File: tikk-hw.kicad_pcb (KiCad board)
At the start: 4 copper layers, 18.1 x 39 mm, 142 parts, among them J1 51281-0598, P6 ZX-SH1.0-4PWT, SW1 TS24CA, SW2 TS24CA, U1 IS31FL3731-QFLS2-TR, U2 LIS2DH12TR, U3 Tenstar nRF52840, U4 CP6208DTR(XBLW), U5 TMP102AIDRLR, U6 CP6208DTR(XBLW)

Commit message: finished initial layout
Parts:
- added C3: CC0402KRX7R7BB104, easyeda2kicad:C0402, F.Cu at (167.6, 108.7)
- added R3: RC0402FR-0720KL, easyeda2kicad:R0402, F.Cu at (168.1, 112.9)
- added R4: RC0402FR-0720KL, easyeda2kicad:R0402, F.Cu at (158.7, 121.4)
- added R5: RC0402FR-0720KL, easyeda2kicad:R0402, F.Cu at (158.3, 116.4)
- added R6: RC0402FR-07100KL, easyeda2kicad:R0402, F.Cu at (160.5, 106.3)
- added R7: RC0402FR-070RL, easyeda2kicad:R0402, F.Cu at (160.5, 107.5)
- moved TP4 20.2 mm to (163.7, 118.0)
- moved TP1 14.8 mm to (168.5, 118.6)
- moved TP3 14.1 mm to (168.5, 116.6)
- moved C10 5.61 mm to (166.3, 104.6)
- moved C12 0.86 mm to (163.1, 114.5), turned to 90 degrees
- moved C14 0.71 mm to (165.4, 117.3)
- moved C13 0.71 mm to (162.0, 117.3)
- moved C11 0.66 mm to (160.0, 118.6), turned to 180 degrees
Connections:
- C10 pad 1: unconnected-(C10-Pad1) -> EXT_VCC
- C10 pad 2: unconnected-(C10-Pad2) -> GND
- C11 pad 1: unconnected-(C11-Pad1) -> EXT_VCC
- C11 pad 2: unconnected-(C11-Pad2) -> GND
- C12 pad 2: Net-(U1-VCC) -> EXT_VCC
- C2 pad 2: Net-(U1-VCC) -> EXT_VCC
- P6 pad 1: unconnected-(P6-Pad1) -> SCL
- P6 pad 2: unconnected-(P6-Pad2) -> SDA
- P6 pad 3: unconnected-(P6-Pad3) -> EXT_VCC
- P6 pad 4: unconnected-(P6-Pad4) -> GND
- P6 pad 5: unconnected-(P6-Pad5) -> GND
- P6 pad 6: unconnected-(P6-Pad6) -> GND
- SW1 pad 1: unconnected-(SW1-Pad1) -> GND
- SW1 pad 4: RESET -> USER
- SW2 pad 1: unconnected-(SW2-Pad1) -> GND
- U1 pad 16: unconnected-(U1-C_FILT-Pad16) -> Net-(U1-C_FILT)
- U1 pad 18: unconnected-(U1-AD-Pad18) -> GND
- U1 pad 2: Net-(U1-VCC) -> EXT_VCC
- U1 pad 29: unconnected-(U1-EP-Pad29) -> GND
- U1 pad 6: unconnected-(U1-R-EXT-Pad6) -> Net-(U1-R-EXT)
- U2 pad 1: unconnected-(U2-SCL/SPC-Pad1) -> SCL
- U2 pad 10: unconnected-(U2-VDD_IO-Pad10) -> EXT_VCC
- U2 pad 11: unconnected-(U2-INT2-Pad11) -> IMU_INT_2
- U2 pad 12: unconnected-(U2-INT1-Pad12) -> IMU_INT_1
- U2 pad 2: unconnected-(U2-CS-Pad2) -> Net-(U2-CS)
- U2 pad 3: unconnected-(U2-SDO/SA0-Pad3) -> Net-(U2-SDO/SA0)
- U2 pad 4: unconnected-(U2-SDA/SDI/SDO-Pad4) -> SDA
- U2 pad 5: unconnected-(U2-RES-Pad5) -> GND
- U2 pad 6: unconnected-(U2-GND-Pad6) -> GND
- U2 pad 7: unconnected-(U2-GND-Pad7) -> GND
- U2 pad 8: unconnected-(U2-GND-Pad8) -> GND
- U2 pad 9: unconnected-(U2-VDD-Pad9) -> EXT_VCC
- U3 pad 10: /P1.11 -> TMP102_ALERT
- U3 pad 19: /P0.22 -> IMU_INT_2
- U3 pad 20: /P0.24 -> IMU_INT_1
- U3 pad 22: /P0.13 -> USER
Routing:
- net SDA: track 0.00 -> 49.6 mm, vias 0 -> 3
- net SCL: track 0.00 -> 45.9 mm, vias 0 -> 6
- net /CB1: track 10.4 -> 36.2 mm, vias 0 -> 8
- net /CB3: track 10.4 -> 35.6 mm, vias 0 -> 10
- net /CB2: track 10.4 -> 34.7 mm, vias 0 -> 8
- net /CB8: track 0.00 -> 23.9 mm, vias 0 -> 1
- net /CA6: track 28.5 -> 51.9 mm, vias 7 -> 10
- net /CA5: track 27.7 -> 48.0 mm, vias 6 -> 8
- net /CA8: track 11.0 -> 29.7 mm, vias 5 -> 8
- net /CB6: track 10.4 -> 29.0 mm, vias 0 -> 7
- net GND: track 10.5 -> 28.5 mm, vias 16 -> 42
- net NFC2: track 0.00 -> 17.7 mm, vias 0 -> 2
- net EXT_VCC: track 2.28 -> 18.5 mm, vias 3 -> 12
- net /CB5: track 10.4 -> 26.3 mm, vias 0 -> 7
- net /CB4: track 10.4 -> 25.3 mm, vias 0 -> 6
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
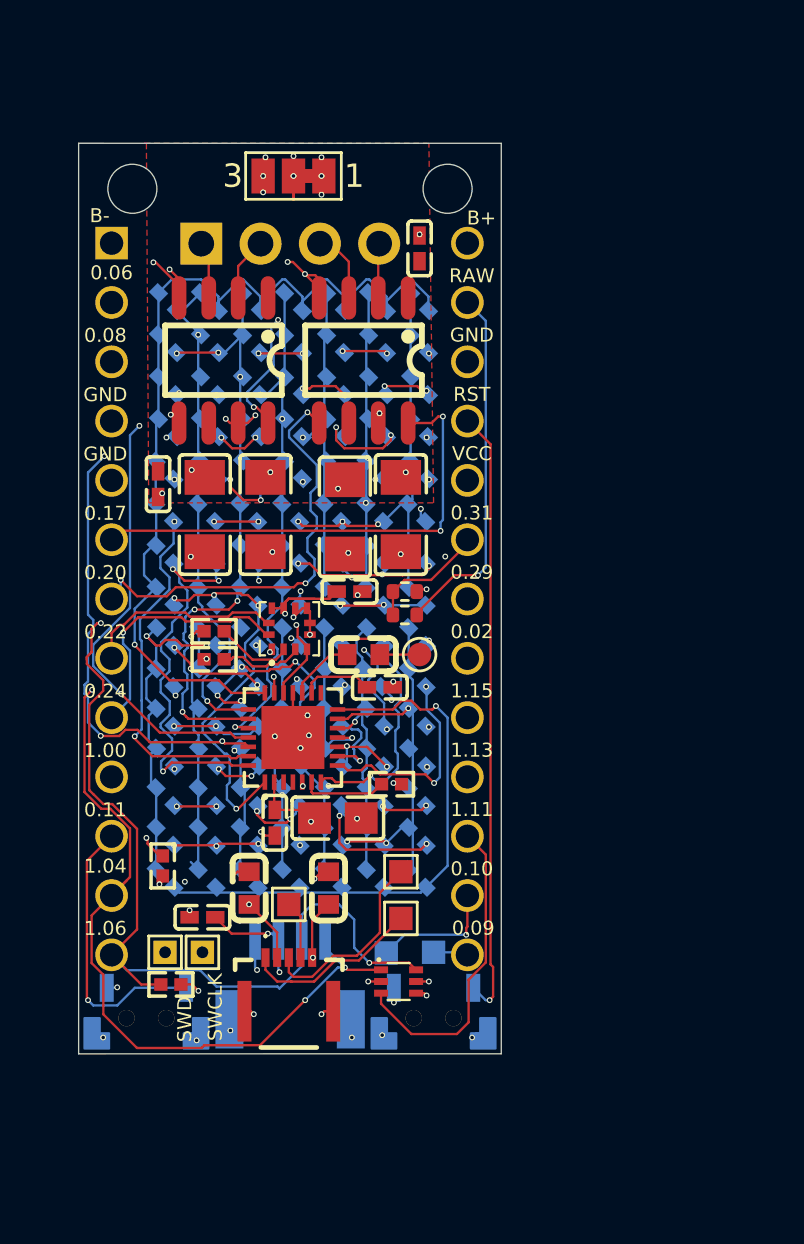
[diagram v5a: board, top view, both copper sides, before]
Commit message: Removed all initial DRC violations
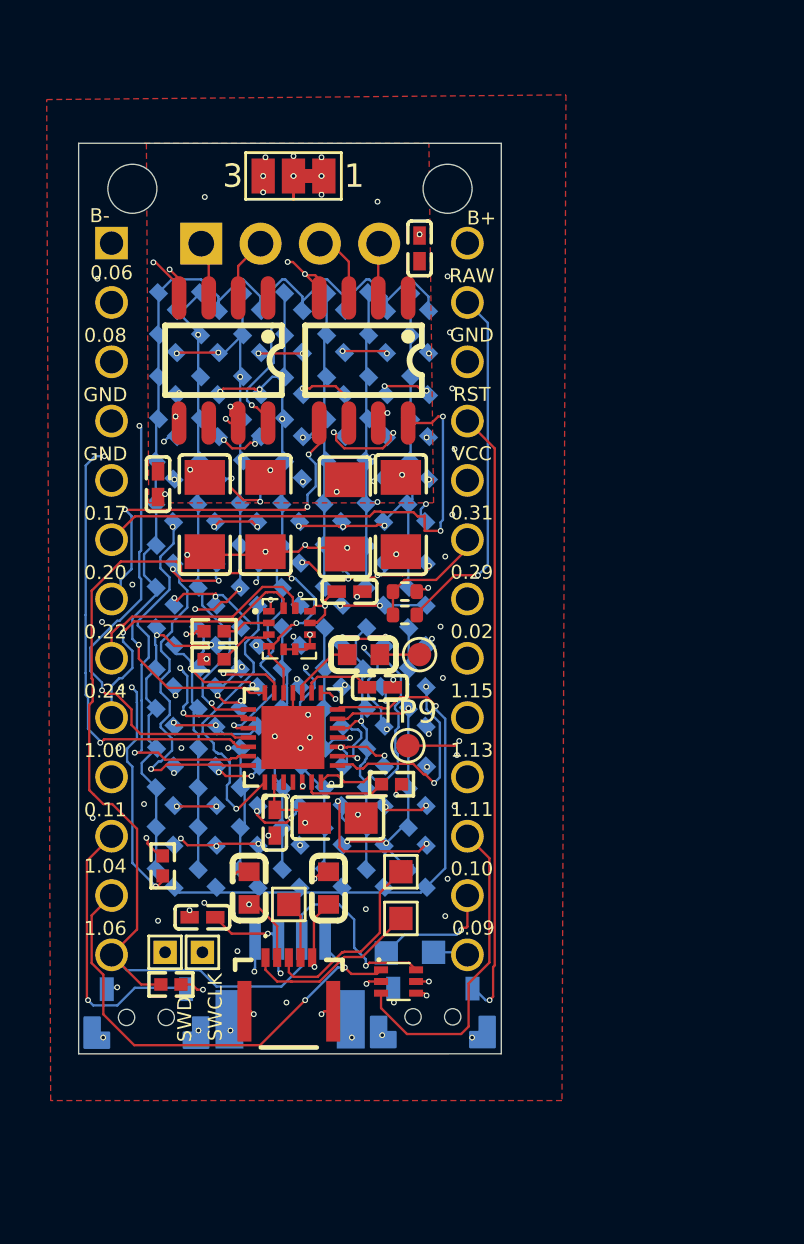
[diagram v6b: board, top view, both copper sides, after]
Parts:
- added TP9: CB9, TestPoint:TestPoint_Pad_D1.0mm, F.Cu at (168.8, 111.2)
- moved SW2 0.06 mm to (169.9, 122.5)
- turned U2 to -90 degrees
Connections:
- SW1 pad 2: (no net) -> GND
- SW2 pad 2: (no net) -> GND
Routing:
- net /CB9: track 0.00 -> 9.10 mm, vias 0 -> 2
- net GND: track 28.5 -> 36.4 mm, vias 42 -> 70
- net SDA: track 49.6 -> 54.7 mm
- net MOTOR2-B: track 18.9 -> 16.3 mm
- net /CA5: track 48.0 -> 50.6 mm
- net /CA7: track 39.0 -> 41.4 mm
- net /CA9: track 25.7 -> 28.1 mm, vias 7 -> 6
- net IMU_INT_2: track 8.51 -> 10.5 mm
- net EXT_VCC: track 18.5 -> 16.7 mm, vias 12 -> 11
- net /CA6: track 51.9 -> 53.3 mm, vias 10 -> 9
- net Net-(U2-SDO/SA0): track 3.76 -> 2.35 mm
- net /CA8: track 29.7 -> 31.1 mm
- net IMU_INT_1: track 11.1 -> 12.4 mm
- net SCL: track 45.9 -> 44.7 mm
- net Net-(U2-CS): track 3.29 -> 2.06 mm
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- added copper zone on F.Cu, net GND
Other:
- rule pad_to_mask_clearance: 0 -> 0.038
- rule solder_mask_min_width: 0.25 -> 0.1

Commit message: updated to add silkscreen qr code area and optimized component info
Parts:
- R1, R2: value 100K -> RC0402FR-07100KL
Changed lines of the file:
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@@
 		(model "${EASYEDA2KICAD}/easyeda2kicad.3dshapes/C0603_L1.6-W0.8-H0.8.wrl"
 			(offset
-				(xyz 0 0 -0)
+				(xyz 0 0 0.4)
 			)
 			(scale
@@
 		(model "${EASYEDA2KICAD}/easyeda2kicad.3dshapes/C1206_L3.2-W1.6-H1.3.wrl"
 			(offset
-				(xyz 0 -0 -0)
+				(xyz 0 -0 0.65)
 			)
 			(scale
@@
 			)
 			(rotate
-				(xyz 0 0 0)
+				(xyz -0 -0 -0)
 			)
 		)
@@
 			)
 		)
-		(property "Value" "100K"
+		(property "Value" "RC0402FR-07100KL"
 			(at 0 1.17 0)
 			(layer "F.Fab")
@@
 		(model "${EASYEDA2KICAD}/easyeda2kicad.3dshapes/C1206_L3.2-W1.6-H1.3.wrl"
 			(offset
-				(xyz 0 -0 -0)
+				(xyz 0 -0 0.65)
 			)
 			(scale
@@
 			)
 			(rotate
-				(xyz 0 0 0)
+				(xyz -0 -0 -0)
 			)
 		)
@@
 		(sheetname "/")
 		(sheetfile "tikk-hw.kicad_sch")
-		(attr exclude_from_pos_files)
+		(attr exclude_from_pos_files exclude_from_bom dnp)
 		(fp_line
 			(start -0.7 -0.7)
@@
 		(sheetname "/")
 		(sheetfile "tikk-hw.kicad_sch")
-		(attr exclude_from_pos_files)
+		(attr exclude_from_pos_files exclude_from_bom dnp)
 		(fp_line
 			(start -0.7 -0.7)
@@
 		(sheetname "/")
 		(sheetfile "tikk-hw.kicad_sch")
-		(attr exclude_from_pos_files)
+		(attr exclude_from_pos_files exclude_from_bom dnp)
 		(fp_circle
 			(center 0 0)
@@
 		(sheetfile "tikk-hw.kicad_sch")
 		(zone_connect 2)
-		(attr exclude_from_pos_files exclude_from_bom allow_soldermask_bridges)
+		(attr exclude_from_pos_files exclude_from_bom dnp allow_soldermask_bridges)
 		(net_tie_pad_groups "1, 2")
 		(fp_poly
@@
 		(model "${EASYEDA2KICAD}/easyeda2kicad.3dshapes/C1206_L3.2-W1.6-H1.3.wrl"
 			(offset
-				(xyz 0 -0 -0)
+				(xyz 0 -0 0.65)
 			)
 			(scale
@@
 			)
 			(rotate
-				(xyz 0 0 0)
+				(xyz -0 -0 -0)
 			)
 		)
@@
 		(sheetname "/")
 		(sheetfile "tikk-hw.kicad_sch")
-		(attr exclude_from_pos_files)
+		(attr exclude_from_pos_files exclude_from_bom dnp)
 		(fp_circle
 			(center 0 0)
@@
 			)
 		)
-		(property "Value" "100K"
+		(property "Value" "RC0402FR-07100KL"
 			(at 0 1.17 0)
 			(layer "F.Fab")
@@
 		(model "${EASYEDA2KICAD}/easyeda2kicad.3dshapes/C0805_L2.0-W1.3-H1.3.wrl"
 			(offset
-				(xyz 0 -0 -0)
+				(xyz 0 -0 0.65)
 			)
 			(scale
@@
 		(model "${EASYEDA2KICAD}/easyeda2kicad.3dshapes/C0603_L1.6-W0.8-H0.8.wrl"
 			(offset
-				(xyz 0 0 -0)
+				(xyz 0 0 0.4)
 			)
 			(scale
@@
 		(sheetname "/")
 		(sheetfile "tikk-hw.kicad_sch")
-		(attr through_hole)
+		(attr through_hole exclude_from_pos_files exclude_from_bom dnp)
 		(fp_line
 			(start -8.89 -21.59)
@@
 		)
 		(fp_text user "0.11"
-			(at -7.8867 7.7597 0)
+			(at -8.128767 7.912475 45)
 			(layer "F.SilkS")
 			(effects
@@
 		)
 		(fp_text user "1.00"
-			(at -7.8867 5.2197 180)
+			(at -8.028767 5.312475 45)
 			(layer "F.SilkS")
 			(effects
@@
 			)
 		)
+		(property "LCSC" "C18548053"
+			(at 0 0 0)
+			(layer "F.SilkS")
+			(hide yes)
+			(effects
+				(font
+					(size 1.27 1.27)
+					(thickness 0.15)
+				)
+			)
+		)
 		(sheetname "/")
 		(sheetfile "tikk-hw.kicad_sch")
@@
 		(sheetname "/")
 		(sheetfile "tikk-hw.kicad_sch")
-		(attr exclude_from_pos_files)
+		(attr exclude_from_pos_files exclude_from_bom dnp)
 		(fp_line
 			(start -0.7 -0.7)
@@
 		(model "${EASYEDA2KICAD}/easyeda2kicad.3dshapes/C0603_L1.6-W0.8-H0.8.wrl"
 			(offset
-				(xyz 0 0 -0)
+				(xyz 0 0 0.35)
 			)
 			(scale
@@
 		(sheetname "/")
 		(sheetfile "tikk-hw.kicad_sch")
-		(attr exclude_from_pos_files)
+		(attr exclude_from_pos_files exclude_from_bom dnp)
 		(fp_line
 			(start -0.7 -0.7)
@@
 		(model "${EASYEDA2KICAD}/easyeda2kicad.3dshapes/C1206_L3.2-W1.6-H1.3.wrl"
 			(offset
-				(xyz 0 -0 -0)
+				(xyz 0 -0 0.65)
 			)
 			(scale
@@
 			)
 			(rotate
-				(xyz 0 0 0)
+				(xyz -0 -0 -0)
 			)
 		)
@@
 		(sheetname "/")
 		(sheetfile "tikk-hw.kicad_sch")
-		(attr exclude_from_pos_files)
+		(attr exclude_from_pos_files exclude_from_bom dnp)
 		(fp_line
 			(start -0.7 -0.7)
@@
 		(model "${EASYEDA2KICAD}/easyeda2kicad.3dshapes/SW-SMD_TS24CA.wrl"
 			(offset
-				(xyz -0 0.68 0.4)
+				(xyz -0 0.68 1.5)
 			)
 			(scale
@@
 			)
 			(rotate
-				(xyz 0 0 0)
+				(xyz -0 -0 -0)
 			)
 		)
@@
 		(sheetname "/")
 		(sheetfile "tikk-hw.kicad_sch")
-		(attr exclude_from_pos_files)
+		(attr exclude_from_pos_files exclude_from_bom dnp)
 		(fp_line
 			(start 0.7 0.7)
@@
 		(sheetname "/")
 		(sheetfile "tikk-hw.kicad_sch")
-		(attr exclude_from_pos_files)
+		(attr exclude_from_pos_files exclude_from_bom dnp)
 		(fp_line
 			(start 0.7 0.7)
@@
 		(sheetname "/")
 		(sheetfile "tikk-hw.kicad_sch")
-		(attr exclude_from_pos_files exclude_from_bom)
+		(attr exclude_from_pos_files exclude_from_bom dnp)
 		(fp_circle
 			(center 0 0)
@@
 		(model "${EASYEDA2KICAD}/easyeda2kicad.3dshapes/SW-SMD_TS24CA.wrl"
 			(offset
-				(xyz -0 0.68 0.4)
+				(xyz -0 0.68 1.5)
 			)
 			(scale
@@
 			)
 			(rotate
-				(xyz 0 0 0)
+				(xyz -0 -0 -0)
 			)
 		)
@@
 		(sheetname "/")
 		(sheetfile "tikk-hw.kicad_sch")
-		(attr exclude_from_pos_files exclude_from_bom)
+		(attr exclude_from_pos_files exclude_from_bom dnp)
 		(fp_circle
 			(center 0 0)
@@
 		)
 	)
+	(gr_circle
+		(center 162.102533 113.302775)
+		(end 162.202533 113.202775)
+		(stroke
+			(width 0.1)
+			(type solid)
+		)
+		(fill yes)
+		(layer "F.SilkS")
+	)
+	(gr_rect
+		(start 156.602533 109.902775)
+		(end 161.602533 114.902775)
+		(stroke
+			(width 0.1)
+			(type solid)
+		)
+		(fill yes)
+		(layer "F.SilkS")
+	)
 	(gr_line

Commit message: add fiducials for mfg
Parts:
- added FID1: Fiducial, Fiducial:Fiducial_0.5mm_Mask1mm, F.Cu at (160.0, 86.4)
- added FID2: Fiducial, Fiducial:Fiducial_0.5mm_Mask1mm, F.Cu at (155.6, 123.5)
- added FID3: Fiducial, Fiducial:Fiducial_0.5mm_Mask1mm, F.Cu at (171.8, 123.5)
- added FID4: Fiducial, Fiducial:Fiducial_0.5mm_Mask1mm, B.Cu at (167.0, 86.5)
- added FID5: Fiducial, Fiducial:Fiducial_0.5mm_Mask1mm, B.Cu at (160.2, 86.2)
- added FID6: Fiducial, Fiducial:Fiducial_0.5mm_Mask1mm, B.Cu at (168.6, 118.3)
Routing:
- net GND: track 36.4 -> 42.0 mm
- net MOTOR-PWR: track 5.95 -> 3.10 mm
- net TMP102_ALERT: track 13.9 -> 11.3 mm
- net SCL: track 44.7 -> 43.7 mm
